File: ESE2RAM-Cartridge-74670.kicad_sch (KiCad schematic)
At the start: 26 parts, among them IC1 SRAM, IC2 SRAM, J1 BUS_MSX, U1 74HC670, U2 74HC670, U3 74HC138, U4 74HC00, U5 74HC32

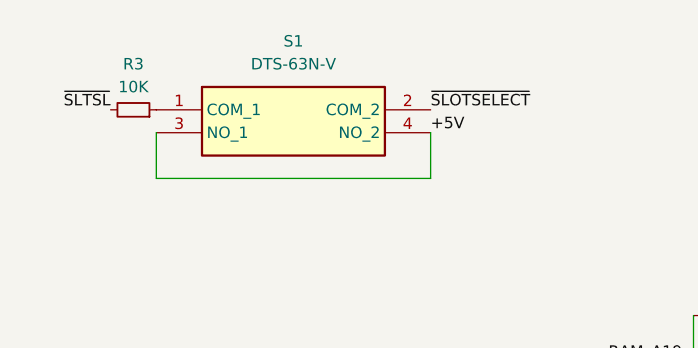
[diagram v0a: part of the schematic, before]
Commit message: Modified schematic
Modified schematic
Change tactile switch.
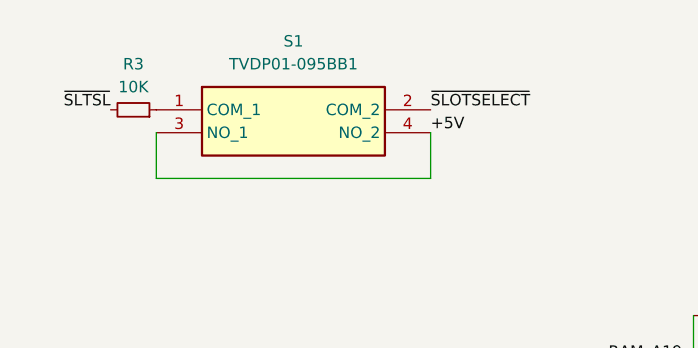
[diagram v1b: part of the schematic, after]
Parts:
- S1: value DTS-63N-V -> TVDP01-095BB1
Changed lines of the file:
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@@
       (effects (font (size 1.27 1.27)))
     )
-    (property "Value" "DTS-63N-V" (at 44.45 17.78 0)
+    (property "Value" "TVDP01-095BB1" (at 44.45 17.78 0)
       (effects (font (size 1.27 1.27)))
     )

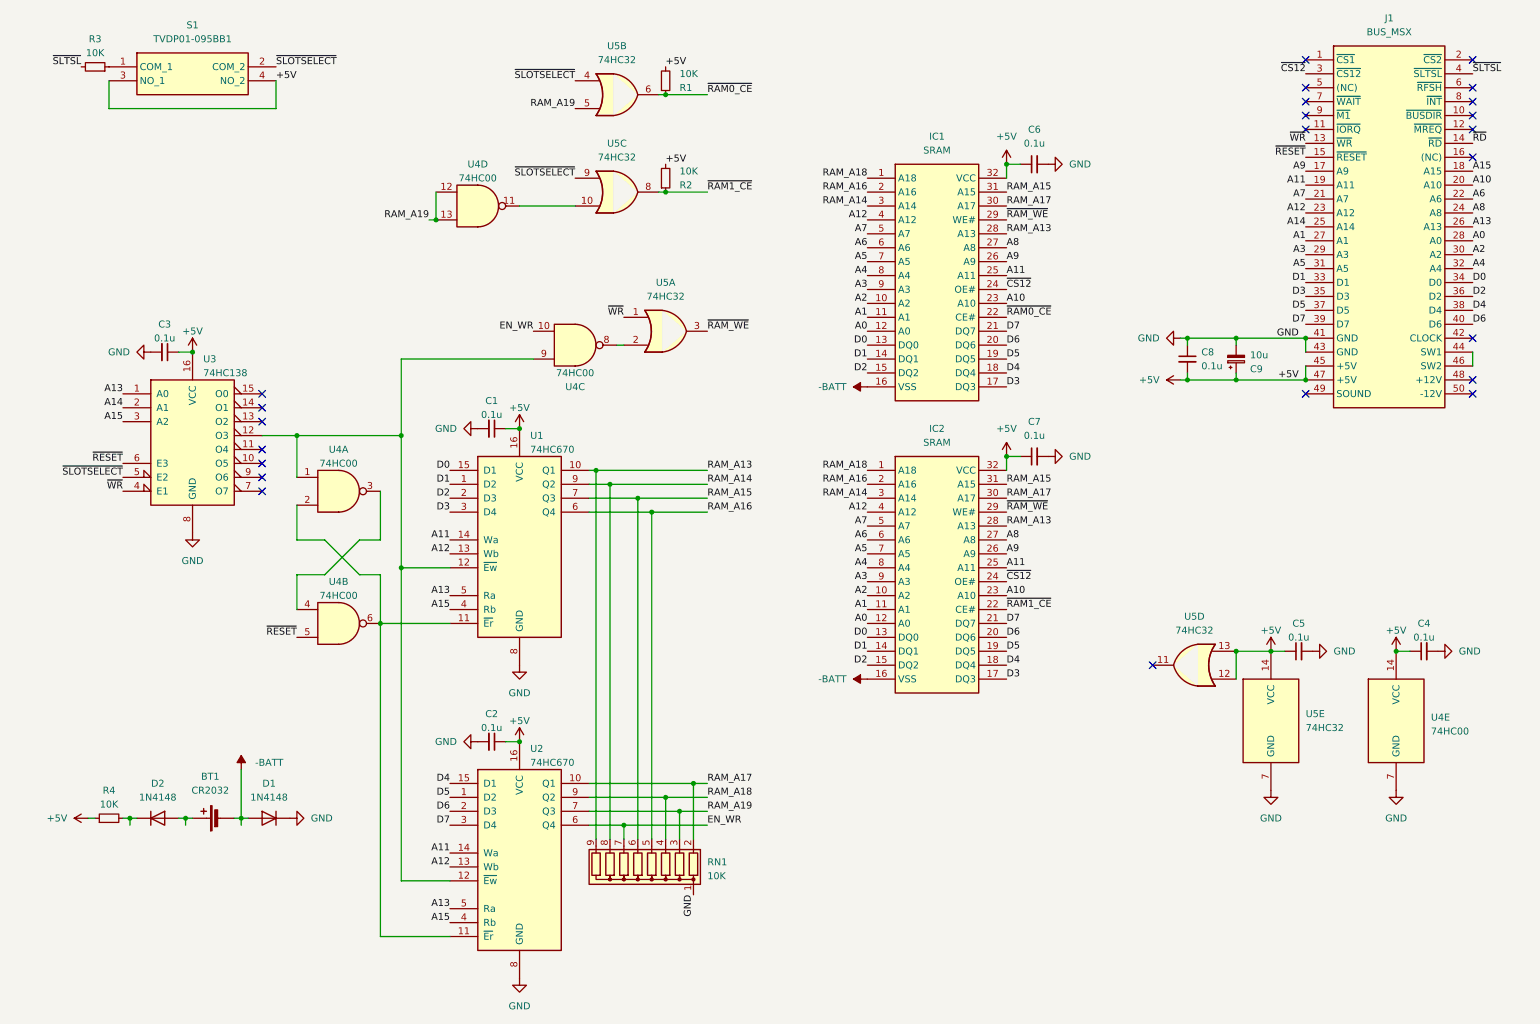
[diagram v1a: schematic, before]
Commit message: Modify Schematic
プロジェクトローカルライブラリの設定が抜けていたのを修正。
Fixed missing project local library settings.
その他の細かな修正。
Other minor corrections.
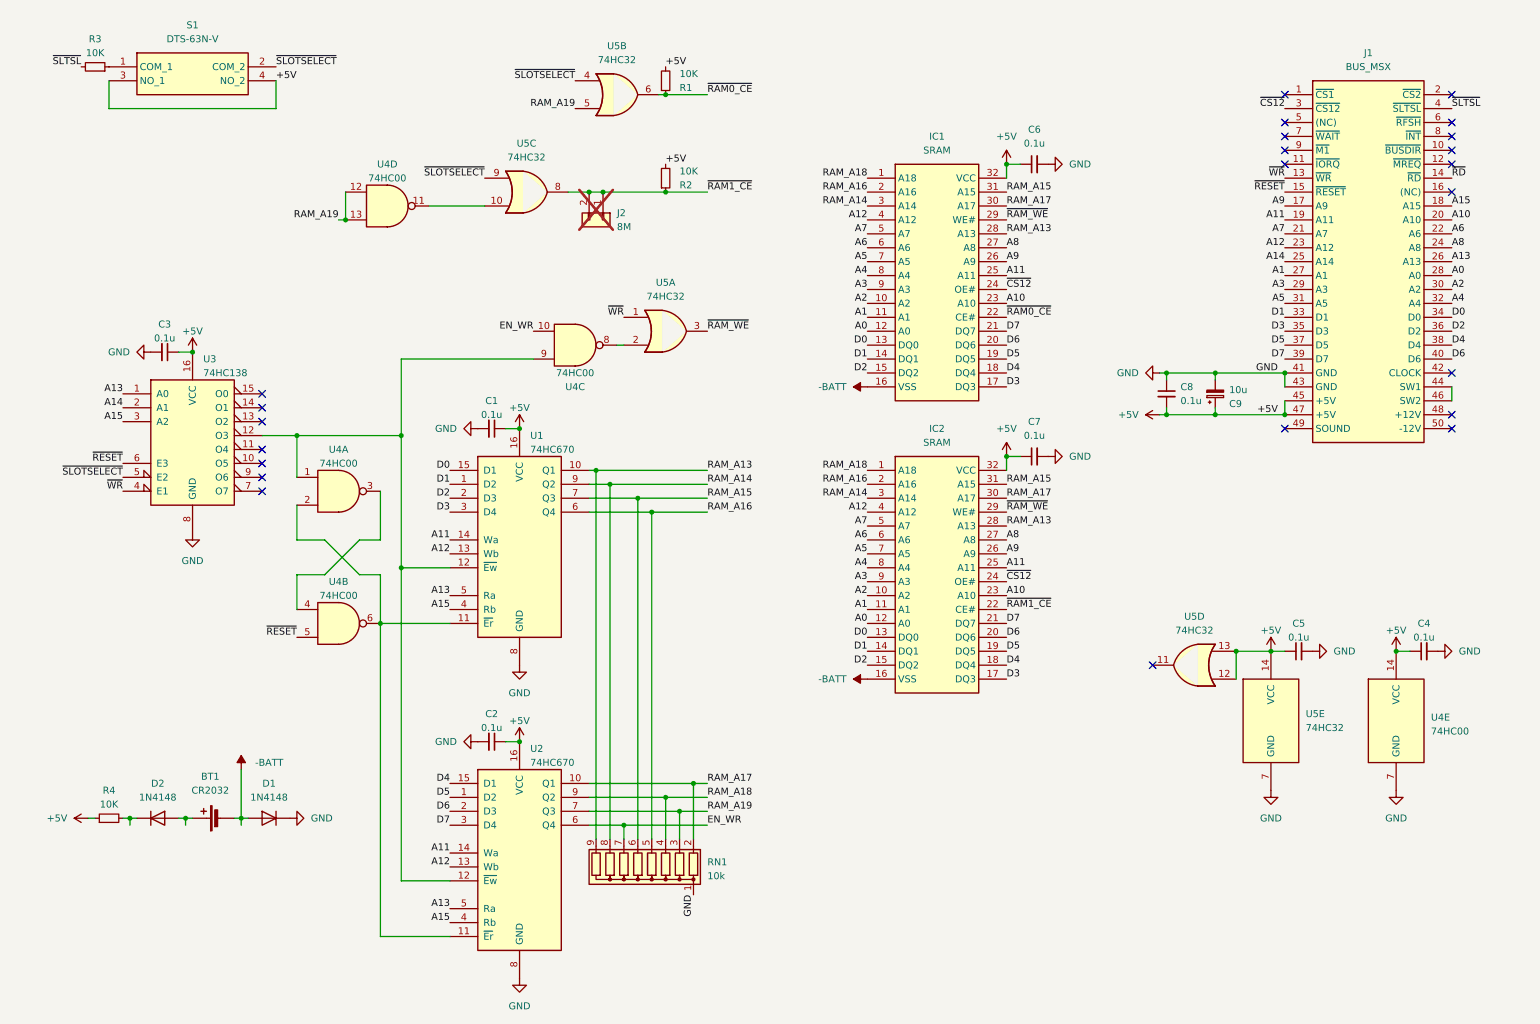
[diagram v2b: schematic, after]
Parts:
- added J2: 8M, Connector_PinHeader_2.00mm:PinHeader_1x02_P2.00mm_Vertical, symbol Connector_Generic:Conn_01x02
- IC1, IC2: symbol ProjectLibrary:SRAM -> SamacSys_Parts:AS6C4008-55PIN
- J1: now left out of the parts list
- RN1: value 10K -> 10k
- S1: value TVDP01-095BB1 -> DTS-63N-V
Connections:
- net ~{RAM1_CE}: now also J2.1 (Pin_1), J2.2 (Pin_2)
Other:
- moved on the sheet: C8, C9, U4D, U5C

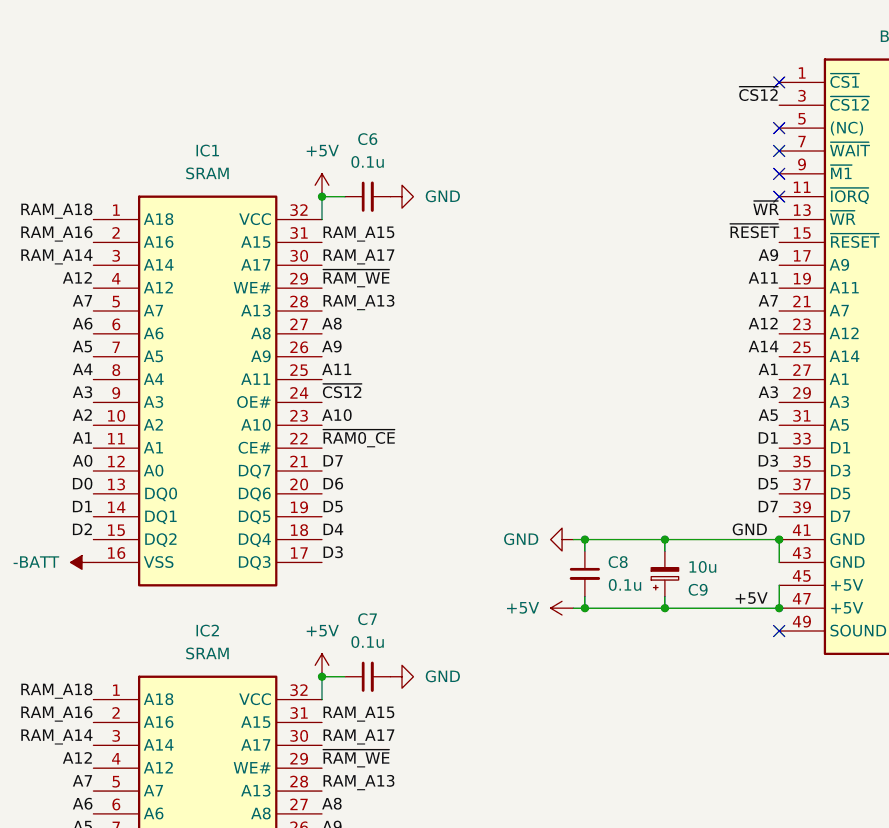
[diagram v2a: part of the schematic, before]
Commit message: Modified Schematic
電解コンデンサの容量を10μFから47μFに変更
電池ソケットのシルク印刷の切り欠き位置が間違っていたのを修正
不要なファイルの削除
その他細かな修正
Changed the capacitance of electrolytic capacitor from 10uF to 47uF.
Fixed an issue where the notch position on the silkscreen print on the battery socket was incorrect.
Delete unnecessary files.
Other minor corrections.
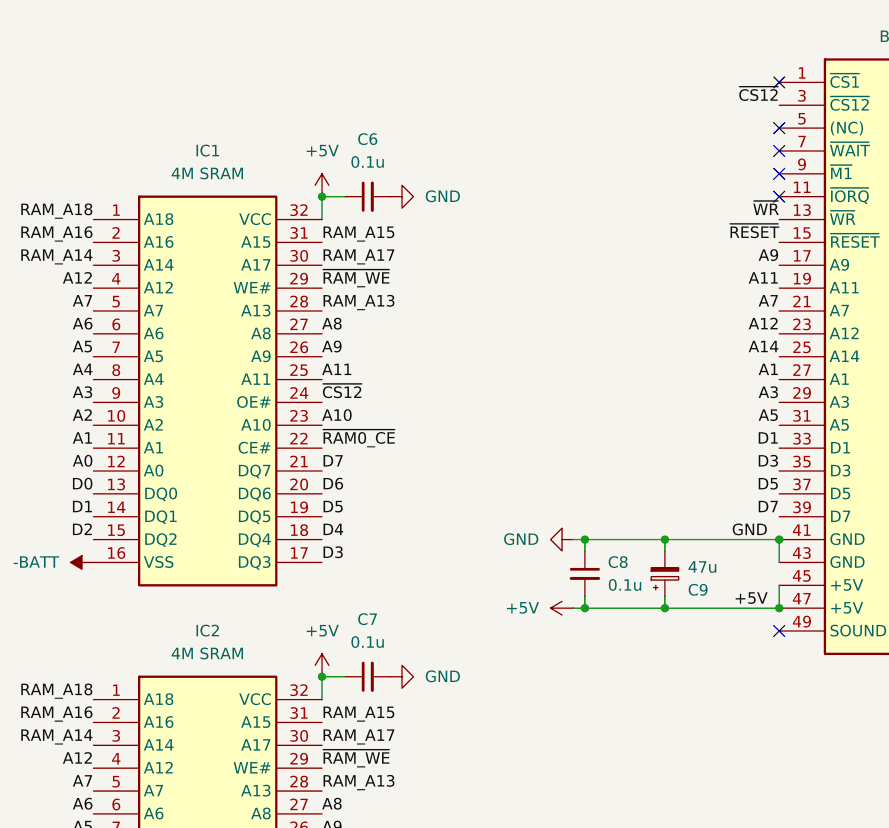
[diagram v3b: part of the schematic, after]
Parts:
- C9: value 10u -> 47u
- IC1, IC2: value SRAM -> 4M SRAM
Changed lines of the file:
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@@
       (effects (font (size 1.27 1.27)))
     )
-    (property "Value" "SRAM" (at 180.34 91.44 0)
+    (property "Value" "4M SRAM" (at 180.34 91.44 0)
       (effects (font (size 1.27 1.27)))
     )
@@
       (effects (font (size 1.27 1.27)) (justify left))
     )
-    (property "Value" "10u" (at 233.68 81.8261 0)
+    (property "Value" "47u" (at 233.68 81.8261 0)
       (effects (font (size 1.27 1.27)) (justify left))
     )
@@
       (effects (font (size 1.27 1.27)))
     )
-    (property "Value" "SRAM" (at 180.34 38.1 0)
-      (effects (font (size 1.27 1.27)))
-    )
+    (property "Value" "4M SRAM" (at 180.34 38.1 0)
+      (effects (font (size 1.27 1.27)))
+    )

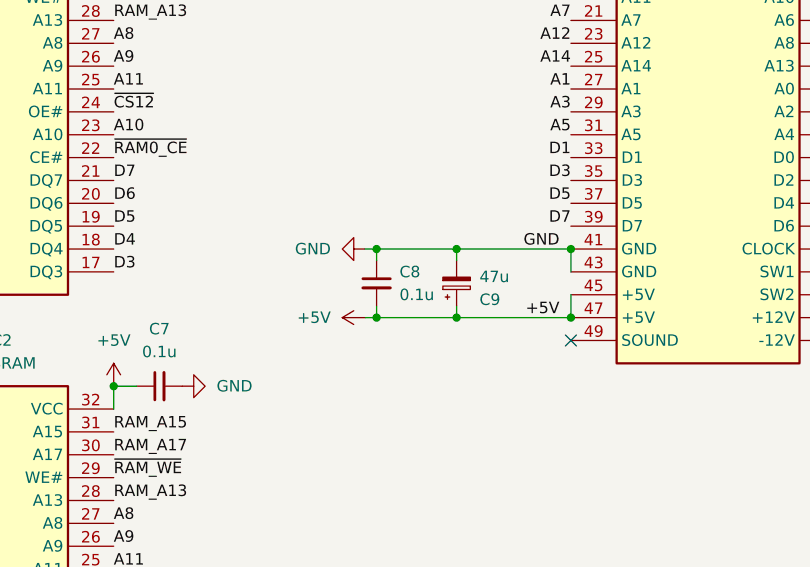
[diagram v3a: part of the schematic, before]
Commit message: Modified Schematic
部品の配置およびフットプリントの修正と、ガーバーデータへの反映
Modify part placement and footprint and reflect in Gerber data.
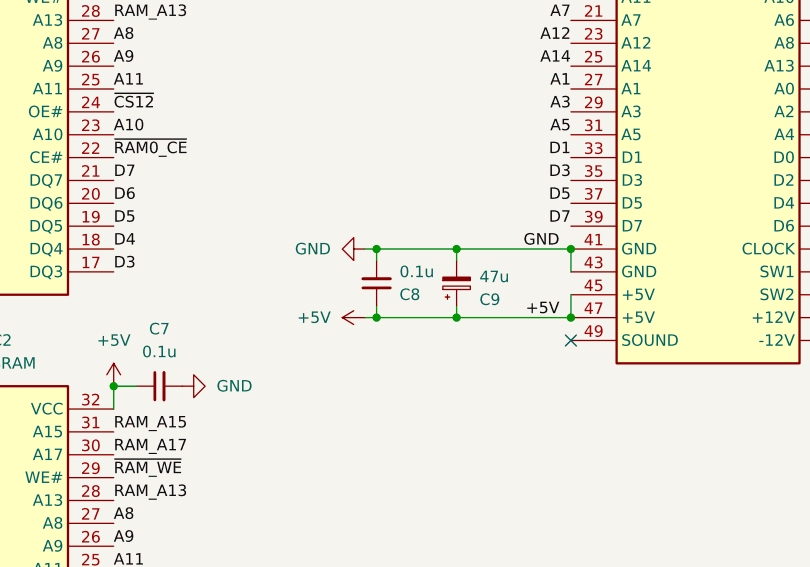
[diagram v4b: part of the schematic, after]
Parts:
- C9: footprint Capacitor_THT:CP_Radial_D5.0mm_P2.00mm -> ProjectLibrary:CP_Radial_D5.0mm_P2.00mm_Horizontal
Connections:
- net +5V: now also C8.1; no longer C8.2
- net GND: now also C8.2; no longer C8.1
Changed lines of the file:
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@@
   (title_block
     (title "ESE2RAM Cartridge (74x670 version)")
-    (date "2024-04-05")
-    (rev "3")
+    (date "2024-04-13")
+    (rev "4")
     (company "Goripon Hardware")
   )
@@
     )
   )
-  (symbol (lib_id "Device:C_Small") (at 222.25 82.55 0) (unit 1)
+  (symbol (lib_id "Device:C_Small") (at 222.25 82.55 0) (mirror x) (unit 1)
     (in_bom yes) (on_board yes) (dnp no)
-    (property "Reference" "C8" (at 224.79 81.2863 0)
+    (property "Reference" "C8" (at 224.79 83.8137 0)
       (effects (font (size 1.27 1.27)) (justify left))
     )
-    (property "Value" "0.1u" (at 224.79 83.8263 0)
+    (property "Value" "0.1u" (at 224.79 81.2737 0)
       (effects (font (size 1.27 1.27)) (justify left))
     )
@@
       (effects (font (size 1.27 1.27)) (justify left))
     )
-    (property "Footprint" "Capacitor_THT:CP_Radial_D5.0mm_P2.00mm" (at 231.14 82.55 0)
-      (effects (font (size 1.27 1.27)) hide)
-    )
+    (property "Footprint" "ProjectLibrary:CP_Radial_D5.0mm_P2.00mm_Horizontal" (at 231.14 82.55 0)
+      (effects (font (size 1.27 1.27)) hide)
+    )

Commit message: Updated Schematic & Gerber data
回路図データとガーバーデータを更新
Updated Schematic & Gerber data.
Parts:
- J1: footprint ProjectLibrary:BUS_MSX_SHORT_CARD -> ProjectLibrary:BUS_MSX_CARD_SHORT
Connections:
- net +5V: now also C8.2; no longer C8.1
- net GND: now also C8.1; no longer C8.2
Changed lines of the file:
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@@
       (effects (font (size 1.27 1.27)))
     )
-    (property "Footprint" "ProjectLibrary:BUS_MSX_SHORT_CARD" (at 259.08 66.04 0)
+    (property "Footprint" "ProjectLibrary:BUS_MSX_CARD_SHORT" (at 259.08 66.04 0)
       (effects (font (size 1.27 1.27)) hide)
     )
@@
     )
   )
-  (symbol (lib_id "Device:C_Small") (at 222.25 82.55 0) (mirror x) (unit 1)
+  (symbol (lib_id "Device:C_Small") (at 222.25 82.55 0) (unit 1)
     (in_bom yes) (on_board yes) (dnp no)
-    (property "Reference" "C8" (at 224.79 83.8137 0)
-      (effects (font (size 1.27 1.27)) (justify left))
-    )
-    (property "Value" "0.1u" (at 224.79 81.2737 0)
-      (effects (font (size 1.27 1.27)) (justify left))
-    )
+    (property "Reference" "C8" (at 224.79 81.2863 0)
+      (effects (font (size 1.27 1.27)) (justify left))
+    )
+    (property "Value" "0.1u" (at 224.79 83.8263 0)
+      (effects (font (size 1.27 1.27)) (justify left))
+    )
